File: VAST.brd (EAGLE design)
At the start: 160 x 100 mm, 5 parts, among them U2 MPL3115A2

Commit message: Add files via upload
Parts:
- removed U2: MPL3115A2, SparkFun-Sensors:LGA-8-5X3
- added J4: (no value), SparkFun-Connectors:MOLEX-1X4
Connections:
- removed net CAP: U2.2
- removed net N$18: J1.1, J2.1, U$1.3.3V, U$1.3.3V1, U2.1
- removed net VDDIO: U2.4
- net N$1: now also U$1.2
- net N$13: now also J4.1; no longer U2.3
- net N$2: now also J1.1, J2.1, J4.2, U$1.3.3V, U$1.3.3V1; no longer U$1.2
- net N$3: now also J4.3; no longer U2.7
- net N$4: now also J4.4; no longer U2.8
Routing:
- net N$2: track 6.35 -> 200.4 mm
- net N$18: track 127.5 -> 0.00 mm
- net N$1: track 30.5 -> 52.1 mm
- net N$13: track 120.3 -> 138.7 mm
- net N$4: track 14.3 -> 7.62 mm
- net N$3: track 14.2 -> 7.62 mm
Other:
- board size 160 x 100 mm -> 148.6 x 100 mm
- board text added: "Air Pressure Sensor"
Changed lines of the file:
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@@
 <drawing>
 <settings>
-<setting alwaysvectorfont="yes"/>
+<setting alwaysvectorfont="no"/>
 <setting verticaltext="up"/>
 </settings>
-<grid distance="50" unitdist="mil" unit="mil" style="lines" multiple="1" display="no" altdistance="5" altunitdist="mil" altunit="mil"/>
+<grid distance="50" unitdist="mil" unit="mil" style="lines" multiple="1" display="yes" altdistance="5" altunitdist="mil" altunit="mil"/>
 <layers>
 <layer number="1" name="Top" color="4" fill="1" visible="yes" active="yes"/>
@@
 <board>
 <plain>
-<wire x1="0" y1="0" x2="160" y2="0" width="0" layer="20"/>
+<wire x1="11.43" y1="0" x2="160" y2="0" width="0" layer="20"/>
 <wire x1="160" y1="0" x2="160" y2="100" width="0" layer="20"/>
-<wire x1="160" y1="100" x2="0" y2="100" width="0" layer="20"/>
-<wire x1="0" y1="100" x2="0" y2="0" width="0" layer="20"/>
+<wire x1="160" y1="100" x2="11.43" y2="100" width="0" layer="20"/>
+<wire x1="11.43" y1="100" x2="11.43" y2="0" width="0" layer="20"/>
 <text x="87.63" y="44.45" size="1.778" layer="1" rot="R90">EXT_TEMP</text>
 <text x="87.63" y="58.42" size="1.778" layer="1" rot="R90">INT_TEMP</text>
 <text x="107.95" y="39.37" size="1.778" layer="1" rot="R90">VAST SATCOMM</text>
+<text x="146.05" y="38.1" size="1.778" layer="1" rot="R90">Air Pressure Sensor</text>
+<text x="146.05" y="38.1" size="1.778" layer="1" rot="R90">Air Pressure Sensor</text>
+<text x="146.05" y="38.1" size="1.778" layer="1" rot="R90">Air Pressure Sensor</text>
 </plain>
 <attributes>
@@
 <attribute name="VALUE" x="95.504" y="49.149" size="0.6096" layer="27" font="vector" ratio="20" rot="R90" align="top-left"/>
 </element>
-<element name="U2" library="SparkFun-Sensors" package="LGA-8-5X3" value="MPL3115A2" x="140.97" y="50.8" smashed="yes">
-<attribute name="NAME" x="140.97" y="53.467" size="0.6096" layer="25" font="vector" ratio="20" align="bottom-center"/>
-<attribute name="PROD_ID" value="IC-10869" x="140.97" y="50.8" size="1.778" layer="27" display="off"/>
-<attribute name="VALUE" x="140.97" y="48.133" size="0.6096" layer="27" font="vector" ratio="20" align="top-center"/>
-</element>
 <element name="J2" library="SparkFun-Connectors" package="MOLEX-1X3_LOCK" value="" x="92.71" y="60.96" smashed="yes" rot="R90">
 <attribute name="NAME" x="89.281" y="62.103" size="0.6096" layer="25" font="vector" ratio="20" rot="R90"/>
@@
 <attribute name="VALUE" x="118.11" y="59.69" size="1.27" layer="27" font="vector"/>
 </element>
+<element name="J4" library="SparkFun-Connectors" package="MOLEX-1X4" value="" x="137.16" y="45.72" smashed="yes" rot="R90">
+<attribute name="NAME" x="132.588" y="48.006" size="0.6096" layer="25" font="vector" ratio="20" rot="R90"/>
+<attribute name="PROD_ID" value="CONN-08186" x="137.16" y="45.72" size="1.778" layer="27" rot="R90" display="off"/>
+<attribute name="SF_ID" value="PRT-08231" x="137.16" y="45.72" size="1.778" layer="27" rot="R90" display="off"/>
+<attribute name="VALUE" x="140.589" y="48.006" size="0.6096" layer="27" font="vector" ratio="20" rot="R90"/>
+</element>
 </elements>
 <signals>
@@
 <contactref element="J1" pad="3"/>
 <contactref element="J2" pad="3"/>
-<contactref element="U2" pad="3"/>
 <contactref element="U$1" pad="GND"/>
 <contactref element="U$1" pad="GND1"/>
@@
 <wire x1="92.583" y1="57.15" x2="102.87" y2="57.15" width="0.1524" layer="16"/>
 <wire x1="102.87" y1="57.15" x2="102.87" y2="71.12" width="0.1524" layer="16"/>
-<wire x1="139.77" y1="50.175" x2="137.16" y2="50.175" width="0.1524" layer="1"/>
-<wire x1="143.51" y1="69.85" x2="114.3" y2="69.85" width="0.1524" layer="1"/>
-<wire x1="114.3" y1="69.85" x2="114.3" y2="71.12" width="0.1524" layer="1"/>
-<wire x1="137.16" y1="50.175" x2="137.16" y2="46.99" width="0.1524" layer="1"/>
-<wire x1="137.16" y1="46.99" x2="143.51" y2="46.99" width="0.1524" layer="1"/>
-<wire x1="143.51" y1="46.99" x2="143.51" y2="69.85" width="0.1524" layer="1"/>
-<wire x1="137.16" y1="46.99" x2="121.92" y2="38.1" width="0" layer="19" extent="1-1"/>
-</signal>
-<signal name="CAP">
-<contactref element="U2" pad="2"/>
-</signal>
-<signal name="VDDIO">
-<contactref element="U2" pad="4"/>
-</signal>
-<signal name="N$18">
-<contactref element="J1" pad="1"/>
-<contactref element="J2" pad="1"/>
-<contactref element="U2" pad="1"/>
-<contactref element="U$1" pad="3.3V1"/>
-<contactref element="U$1" pad="3.3V"/>
-<wire x1="92.583" y1="60.96" x2="83.82" y2="60.96" width="0.1524" layer="16"/>
-<wire x1="92.583" y1="48.26" x2="83.82" y2="48.26" width="0.1524" layer="16"/>
-<wire x1="83.82" y1="48.26" x2="83.82" y2="60.96" width="0.1524" layer="16"/>
-<wire x1="83.82" y1="60.96" x2="83.82" y2="73.66" width="0.1524" layer="16"/>
-<wire x1="83.82" y1="73.66" x2="133.35" y2="73.66" width="0.1524" layer="16"/>
-<wire x1="133.35" y1="73.66" x2="133.35" y2="66.04" width="0.1524" layer="16"/>
-<wire x1="133.35" y1="66.04" x2="129.54" y2="66.04" width="0.1524" layer="16"/>
-<wire x1="139.77" y1="52.675" x2="139.7" y2="52.675" width="0.1524" layer="1"/>
-<wire x1="139.7" y1="52.675" x2="139.7" y2="66.04" width="0.1524" layer="1"/>
-<wire x1="139.7" y1="66.04" x2="129.54" y2="66.04" width="0.1524" layer="1"/>
-<wire x1="139.7" y1="52.675" x2="119.38" y2="38.1" width="0" layer="19" extent="1-1"/>
+<wire x1="114.3" y1="71.12" x2="114.3" y2="69.85" width="0.1524" layer="1"/>
+<contactref element="J4" pad="1"/>
+<wire x1="114.3" y1="69.85" x2="140.97" y2="69.85" width="0.2032" layer="1"/>
+<wire x1="140.97" y1="69.85" x2="140.97" y2="45.72" width="0.2032" layer="1"/>
+<wire x1="140.97" y1="45.72" x2="137.16" y2="45.72" width="0.2032" layer="1"/>
+<wire x1="137.16" y1="45.72" x2="137.16" y2="35.56" width="0.2032" layer="1"/>
+<wire x1="137.16" y1="35.56" x2="121.92" y2="35.56" width="0.2032" layer="1"/>
+<wire x1="121.92" y1="35.56" x2="121.92" y2="38.1" width="0.2032" layer="1"/>
 </signal>
 <signal name="N$1">
@@
 <wire x1="88.9" y1="58.42" x2="97.79" y2="58.42" width="0.1524" layer="16"/>
 <wire x1="97.79" y1="58.42" x2="97.79" y2="63.5" width="0.1524" layer="16"/>
+<contactref element="U$1" pad="2"/>
+<wire x1="97.79" y1="63.5" x2="97.79" y2="66.04" width="0.2032" layer="1"/>
+<wire x1="97.79" y1="66.04" x2="111.76" y2="66.04" width="0.2032" layer="1"/>
+<wire x1="111.76" y1="66.04" x2="111.76" y2="63.5" width="0.2032" layer="1"/>
+<wire x1="111.76" y1="63.5" x2="114.3" y2="63.5" width="0.2032" layer="1"/>
 </signal>
 <signal name="AGND">
@@
 <signal name="VIN">
 <contactref element="U$1" pad="VIN"/>
-</signal>
-<signal name="N$2">
-<contactref element="R1" pad="2"/>
-<contactref element="U$1" pad="2"/>
-<wire x1="107.95" y1="63.5" x2="114.3" y2="63.5" width="0.1524" layer="16"/>
-</signal>
-<signal name="N$3">
-<contactref element="U2" pad="7"/>
-<contactref element="U$1" pad="18/A4"/>
-<wire x1="129.54" y1="51.425" x2="129.54" y2="50.8" width="0.1524" layer="1"/>
-<wire x1="142.17" y1="51.425" x2="140.5986" y2="51.425" width="0.1524" layer="1"/>
-<wire x1="140.5986" y1="51.425" x2="140.5986" y2="50.9464" width="0.1524" layer="1"/>
-<wire x1="140.5986" y1="50.9464" x2="138.9414" y2="50.9464" width="0.1524" layer="1"/>
-<wire x1="138.9414" y1="50.9464" x2="138.9414" y2="51.425" width="0.1524" layer="1"/>
-<wire x1="138.9414" y1="51.425" x2="129.54" y2="51.425" width="0.1524" layer="1"/>
-</signal>
-<signal name="N$4">
-<contactref element="U2" pad="8"/>
-<contactref element="U$1" pad="19/A5"/>
-<wire x1="142.17" y1="52.675" x2="140.5986" y2="52.675" width="0.1524" layer="1"/>
-<wire x1="140.5986" y1="52.675" x2="140.5986" y2="52.1964" width="0.1524" layer="1"/>
-<wire x1="140.5986" y1="52.1964" x2="129.54" y2="52.1964" width="0.1524" layer="1"/>
-<wire x1="129.54" y1="52.1964" x2="129.54" y2="53.34" width="0.1524" layer="1"/>
 </signal>
 <signal name="GND">
@@
 </polygon>
 </signal>
+<signal name="N$2">
+<contactref element="J1" pad="1"/>
+<contactref element="J2" pad="1"/>
+<contactref element="U$1" pad="3.3V1"/>
+<contactref element="U$1" pad="3.3V"/>
+<contactref element="R1" pad="2"/>
+<wire x1="92.583" y1="60.96" x2="83.82" y2="60.96" width="0.1524" layer="16"/>
+<wire x1="92.583" y1="48.26" x2="83.82" y2="48.26" width="0.1524" layer="16"/>
+<wire x1="83.82" y1="48.26" x2="83.82" y2="60.96" width="0.1524" layer="16"/>
+<wire x1="83.82" y1="60.96" x2="83.82" y2="73.66" width="0.1524" layer="16"/>
+<wire x1="83.82" y1="73.66" x2="133.35" y2="73.66" width="0.1524" layer="16"/>
+<wire x1="107.95" y1="63.5" x2="107.95" y2="60.96" width="0.2032" layer="16"/>
+<wire x1="107.95" y1="60.96" x2="104.14" y2="60.96" width="0.2032" layer="16"/>
+<wire x1="104.14" y1="60.96" x2="104.14" y2="43.18" width="0.2032" layer="16"/>
+<wire x1="83.82" y1="43.18" x2="104.14" y2="43.18" width="0.2032" layer="16"/>
+<wire x1="83.82" y1="43.18" x2="83.82" y2="48.26" width="0.2032" layer="16"/>
+<contactref element="J4" pad="2"/>
+<wire x1="133.35" y1="73.66" x2="133.35" y2="66.04" width="0.2032" layer="16"/>
+<wire x1="133.35" y1="66.04" x2="129.54" y2="66.04" width="0.2032" layer="16"/>
+<wire x1="133.35" y1="66.04" x2="133.35" y2="48.26" width="0.2032" layer="16"/>
+<wire x1="133.35" y1="48.26" x2="137.16" y2="48.26" width="0.2032" layer="16"/>
+<wire x1="104.14" y1="43.18" x2="104.14" y2="35.56" width="0.2032" layer="16"/>
+<wire x1="104.14" y1="35.56" x2="119.38" y2="35.56" width="0.2032" layer="16"/>
+<wire x1="119.38" y1="35.56" x2="119.38" y2="38.1" width="0.2032" layer="16"/>
+</signal>
+<signal name="N$3">
+<contactref element="U$1" pad="18/A4"/>
+<contactref element="J4" pad="3"/>
+<wire x1="129.54" y1="50.8" x2="137.16" y2="50.8" width="0.2032" layer="1"/>
+</signal>
+<signal name="N$4">
+<contactref element="U$1" pad="19/A5"/>
+<contactref element="J4" pad="4"/>
+<wire x1="129.54" y1="53.34" x2="137.16" y2="53.34" width="0.2032" layer="1"/>
+</signal>
 </signals>

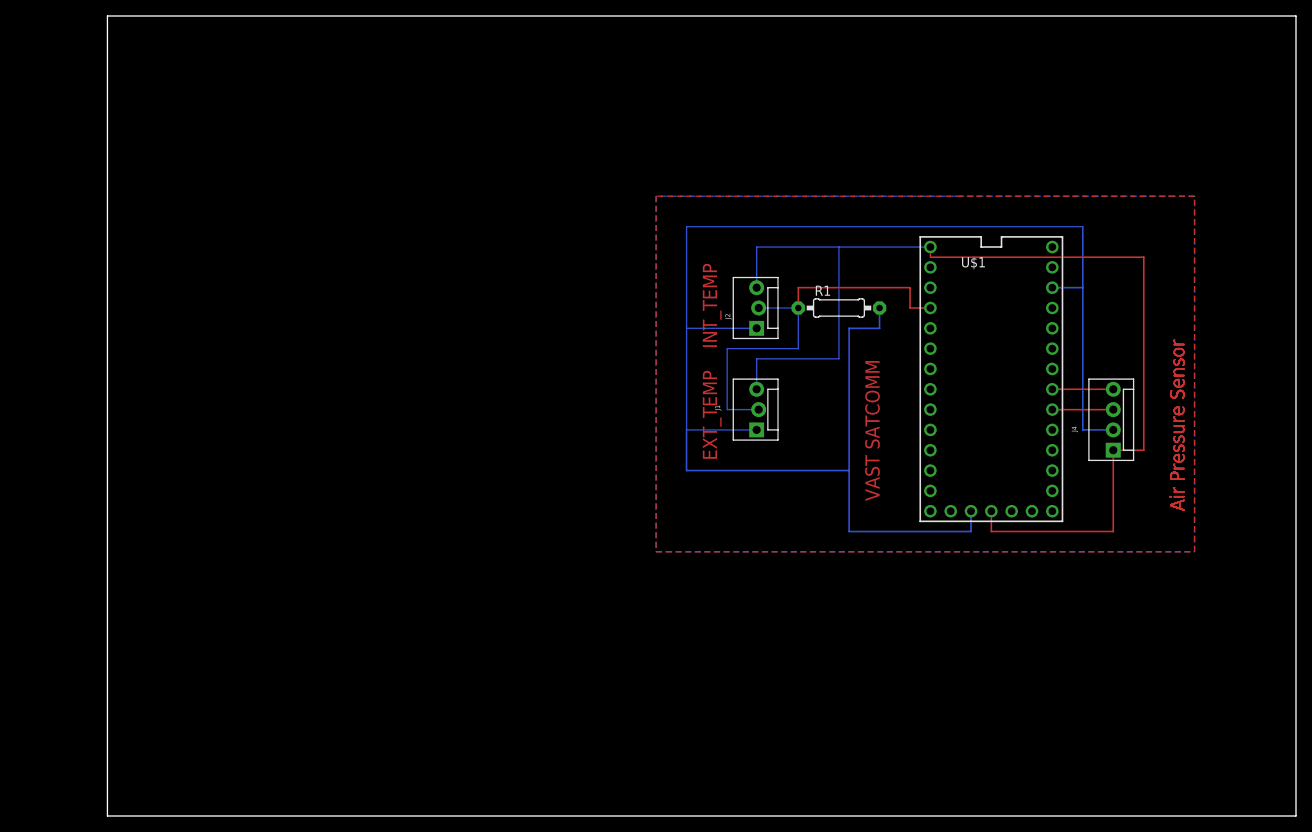
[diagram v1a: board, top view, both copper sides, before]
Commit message: Add files via upload
Updated board with ground VIA and Two Test Pads
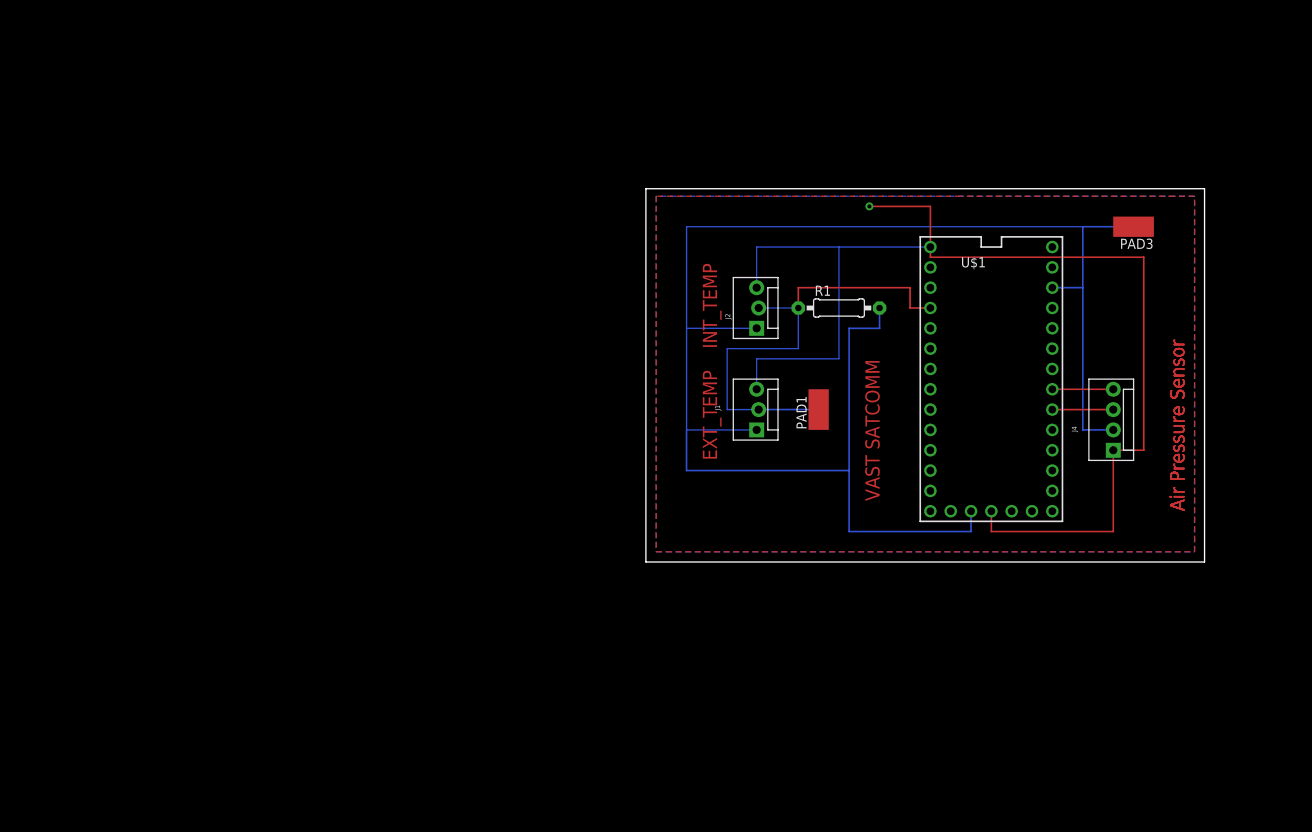
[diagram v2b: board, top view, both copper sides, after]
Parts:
- added PAD1, PAD3: (no value), wirepad:SMD2,54-5,08
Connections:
- net N$1: now also PAD1.1
- net N$2: now also PAD3.1
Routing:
- net N$13: track 138.7 -> 151.4 mm, vias 0 -> 1
- net N$1: track 52.1 -> 59.6 mm
- net N$2: track 200.4 -> 206.8 mm
- added copper zone on layer 1, net N$13
- added copper zone on layer 16, net N$13
- removed copper zone on layer 1, net GND
- removed copper zone on layer 16, net GND
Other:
- board size 148.6 x 100 mm -> 69.8 x 46.7 mm
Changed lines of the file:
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@@
 <board>
 <plain>
-<wire x1="11.43" y1="0" x2="160" y2="0" width="0" layer="20"/>
-<wire x1="160" y1="0" x2="160" y2="100" width="0" layer="20"/>
-<wire x1="160" y1="100" x2="11.43" y2="100" width="0" layer="20"/>
-<wire x1="11.43" y1="100" x2="11.43" y2="0" width="0" layer="20"/>
+<wire x1="78.74" y1="31.75" x2="148.57" y2="31.75" width="0" layer="20"/>
+<wire x1="148.57" y1="31.75" x2="148.57" y2="78.41" width="0" layer="20"/>
+<wire x1="148.57" y1="78.41" x2="78.74" y2="78.41" width="0" layer="20"/>
+<wire x1="78.74" y1="78.41" x2="78.74" y2="31.75" width="0" layer="20"/>
 <text x="87.63" y="44.45" size="1.778" layer="1" rot="R90">EXT_TEMP</text>
 <text x="87.63" y="58.42" size="1.778" layer="1" rot="R90">INT_TEMP</text>
@@
 <attribute name="VALUE" x="140.589" y="48.006" size="0.6096" layer="27" font="vector" ratio="20" rot="R90"/>
 </element>
+<element name="PAD1" library="wirepad" library_urn="urn:adsk.eagle:library:412" package="SMD2,54-5,08" package3d_urn="urn:adsk.eagle:package:30841/1" value="" x="100.33" y="50.8" smashed="yes">
+<attribute name="NAME" x="98.83" y="48.3" size="1.27" layer="25" rot="R90"/>
+<attribute name="POPULARITY" value="21" x="100.33" y="50.8" size="1.778" layer="27" display="off"/>
+<attribute name="VALUE" x="100.33" y="50.8" size="0.0254" layer="27"/>
+</element>
+<element name="PAD3" library="wirepad" library_urn="urn:adsk.eagle:library:412" package="SMD2,54-5,08" package3d_urn="urn:adsk.eagle:package:30841/1" value="" x="139.7" y="73.66" smashed="yes" rot="R90">
+<attribute name="NAME" x="142.2" y="72.16" size="1.27" layer="25" rot="R180"/>
+<attribute name="POPULARITY" value="21" x="139.7" y="73.66" size="1.778" layer="27" rot="R90" display="off"/>
+<attribute name="VALUE" x="139.7" y="73.66" size="0.0254" layer="27" rot="R90"/>
+</element>
 </elements>
 <signals>
@@
 <wire x1="92.583" y1="57.15" x2="102.87" y2="57.15" width="0.1524" layer="16"/>
 <wire x1="102.87" y1="57.15" x2="102.87" y2="71.12" width="0.1524" layer="16"/>
-<wire x1="114.3" y1="71.12" x2="114.3" y2="69.85" width="0.1524" layer="1"/>
 <contactref element="J4" pad="1"/>
-<wire x1="114.3" y1="69.85" x2="140.97" y2="69.85" width="0.2032" layer="1"/>
+<wire x1="140.97" y1="69.85" x2="114.3" y2="69.85" width="0.2032" layer="1"/>
 <wire x1="140.97" y1="69.85" x2="140.97" y2="45.72" width="0.2032" layer="1"/>
 <wire x1="140.97" y1="45.72" x2="137.16" y2="45.72" width="0.2032" layer="1"/>
@@
 <wire x1="137.16" y1="35.56" x2="121.92" y2="35.56" width="0.2032" layer="1"/>
 <wire x1="121.92" y1="35.56" x2="121.92" y2="38.1" width="0.2032" layer="1"/>
-</signal>
-<signal name="N$1">
-<contactref element="J2" pad="2"/>
-<contactref element="J1" pad="2"/>
-<contactref element="R1" pad="1"/>
-<wire x1="92.837" y1="63.5" x2="97.79" y2="63.5" width="0.1524" layer="16"/>
-<wire x1="92.837" y1="50.8" x2="88.9" y2="50.8" width="0.1524" layer="16"/>
-<wire x1="88.9" y1="50.8" x2="88.9" y2="58.42" width="0.1524" layer="16"/>
-<wire x1="88.9" y1="58.42" x2="97.79" y2="58.42" width="0.1524" layer="16"/>
-<wire x1="97.79" y1="58.42" x2="97.79" y2="63.5" width="0.1524" layer="16"/>
-<contactref element="U$1" pad="2"/>
-<wire x1="97.79" y1="63.5" x2="97.79" y2="66.04" width="0.2032" layer="1"/>
-<wire x1="97.79" y1="66.04" x2="111.76" y2="66.04" width="0.2032" layer="1"/>
-<wire x1="111.76" y1="66.04" x2="111.76" y2="63.5" width="0.2032" layer="1"/>
-<wire x1="111.76" y1="63.5" x2="114.3" y2="63.5" width="0.2032" layer="1"/>
-</signal>
-<signal name="AGND">
-<contactref element="U$1" pad="AGND"/>
-</signal>
-<signal name="VBAT">
-<contactref element="U$1" pad="VBAT"/>
-</signal>
-<signal name="VIN">
-<contactref element="U$1" pad="VIN"/>
-</signal>
-<signal name="GND">
 <polygon width="0.1524" layer="1">
 <vertex x="118.11" y="77.47"/>
@@
 <vertex x="147.32" y="77.47"/>
 </polygon>
+<via x="106.68" y="76.2" extent="1-16" drill="0.508"/>
+<wire x1="114.3" y1="69.85" x2="114.3" y2="71.12" width="0.2032" layer="1"/>
+<wire x1="106.68" y1="76.2" x2="114.3" y2="76.2" width="0.2032" layer="1"/>
+<wire x1="114.3" y1="76.2" x2="114.3" y2="71.12" width="0.2032" layer="1"/>
+</signal>
+<signal name="N$1">
+<contactref element="J2" pad="2"/>
+<contactref element="J1" pad="2"/>
+<contactref element="R1" pad="1"/>
+<wire x1="92.837" y1="63.5" x2="97.79" y2="63.5" width="0.1524" layer="16"/>
+<wire x1="92.837" y1="50.8" x2="88.9" y2="50.8" width="0.1524" layer="16"/>
+<wire x1="88.9" y1="50.8" x2="88.9" y2="58.42" width="0.1524" layer="16"/>
+<wire x1="88.9" y1="58.42" x2="97.79" y2="58.42" width="0.1524" layer="16"/>
+<wire x1="97.79" y1="58.42" x2="97.79" y2="63.5" width="0.1524" layer="16"/>
+<contactref element="U$1" pad="2"/>
+<wire x1="97.79" y1="63.5" x2="97.79" y2="66.04" width="0.2032" layer="1"/>
+<wire x1="97.79" y1="66.04" x2="111.76" y2="66.04" width="0.2032" layer="1"/>
+<wire x1="111.76" y1="66.04" x2="111.76" y2="63.5" width="0.2032" layer="1"/>
+<wire x1="111.76" y1="63.5" x2="114.3" y2="63.5" width="0.2032" layer="1"/>
+<contactref element="PAD1" pad="1"/>
+<wire x1="92.837" y1="50.8" x2="100.33" y2="50.8" width="0.2032" layer="16"/>
+<wire x1="100.33" y1="50.8" x2="100.33" y2="50.8" width="0" layer="19" extent="1-16"/>
+</signal>
+<signal name="AGND">
+<contactref element="U$1" pad="AGND"/>
+</signal>
+<signal name="VBAT">
+<contactref element="U$1" pad="VBAT"/>
+</signal>
+<signal name="VIN">
+<contactref element="U$1" pad="VIN"/>
 </signal>
 <signal name="N$2">
@@
 <wire x1="104.14" y1="35.56" x2="119.38" y2="35.56" width="0.2032" layer="16"/>
 <wire x1="119.38" y1="35.56" x2="119.38" y2="38.1" width="0.2032" layer="16"/>
+<contactref element="PAD3" pad="1"/>
+<wire x1="133.35" y1="73.66" x2="139.7" y2="73.66" width="0.2032" layer="16"/>
+<wire x1="139.7" y1="73.66" x2="139.7" y2="73.66" width="0" layer="19" extent="1-16"/>
 </signal>
 <signal name="N$3">
@@
 </board>
 </drawing>
+<compatibility>
+<note version="8.2" severity="warning">
+Since Version 8.2, EAGLE supports online libraries. The ids
+of those online libraries will not be understood (or retained)
+with this version.
+</note>
+<note version="8.3" severity="warning">
+Since Version 8.3, EAGLE supports URNs for individual library
+assets (packages, symbols, and devices). The URNs of those assets
+will not be understood (or retained) with this version.
+</note>
+<note version="8.3" severity="warning">
+Since Version 8.3, EAGLE supports the association of 3D packages
+with devices in libraries, schematics, and board files. Those 3D
+packages will not be understood (or retained) with this version.
+</note>
+</compatibility>
 </eagle>
